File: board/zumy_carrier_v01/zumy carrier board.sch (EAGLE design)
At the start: 16 parts, among them J1 ODROID_POWER, J2 BATT_POWER, M1 POLOLU_STEP_DOWN, M2 ITG/MPU_MODULE, M3 POLOLU_DRV8833_MODULE, SW1 500SSP1S1M6QEA

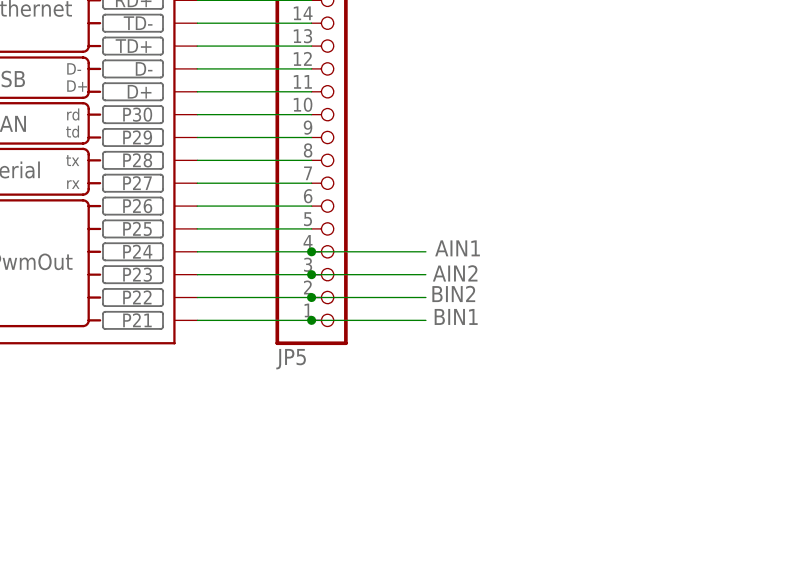
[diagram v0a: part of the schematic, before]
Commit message: Most of Rev D done. Major rearrangement. New mounting hole pattern.
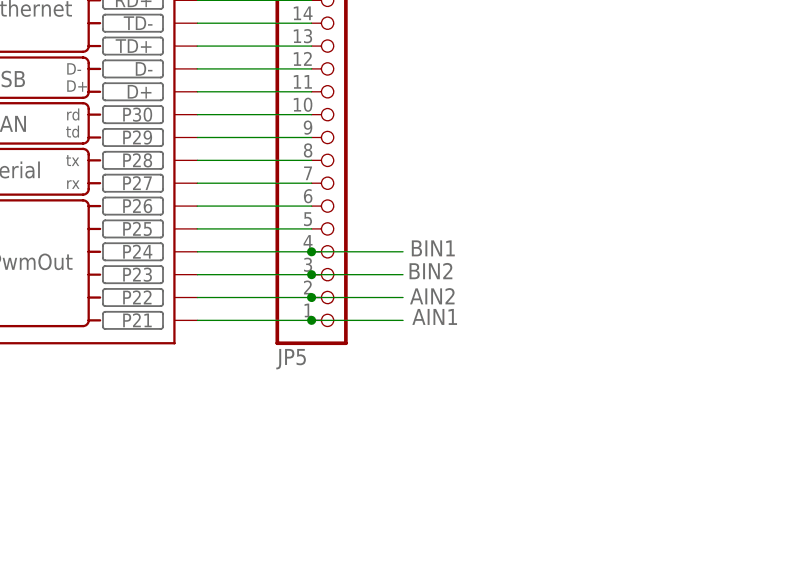
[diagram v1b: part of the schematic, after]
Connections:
- net AIN1: now also JP5.1, KIT1.P21; no longer JP5.4, KIT1.P24
- net AIN2: now also JP5.2, KIT1.P22; no longer JP5.3, KIT1.P23
- net BIN1: now also JP5.4, KIT1.P24; no longer JP5.1, KIT1.P21
- net BIN2: now also JP5.3, KIT1.P23; no longer JP5.2, KIT1.P22
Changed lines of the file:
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@@
 </segment>
 <segment>
-<pinref part="JP5" gate="A" pin="1"/>
-<wire x1="167.64" y1="58.42" x2="180.34" y2="58.42" width="0.1524" layer="91"/>
-<wire x1="180.34" y1="58.42" x2="193.04" y2="58.42" width="0.1524" layer="91"/>
-<junction x="180.34" y="58.42"/>
-<label x="193.802" y="57.912" size="1.778" layer="95"/>
-<pinref part="KIT1" gate="KIT" pin="P21"/>
+<pinref part="JP5" gate="A" pin="4"/>
+<wire x1="167.64" y1="66.04" x2="180.34" y2="66.04" width="0.1524" layer="91"/>
+<pinref part="KIT1" gate="KIT" pin="P24"/>
+<wire x1="180.34" y1="66.04" x2="190.5" y2="66.04" width="0.1524" layer="91"/>
+<label x="191.262" y="65.532" size="1.778" layer="95"/>
+<junction x="180.34" y="66.04"/>
 </segment>
 </net>
@@
 </segment>
 <segment>
-<pinref part="JP5" gate="A" pin="2"/>
-<wire x1="167.64" y1="60.96" x2="180.34" y2="60.96" width="0.1524" layer="91"/>
-<wire x1="180.34" y1="60.96" x2="193.04" y2="60.96" width="0.1524" layer="91"/>
-<junction x="180.34" y="60.96"/>
-<label x="193.548" y="60.452" size="1.778" layer="95"/>
-<pinref part="KIT1" gate="KIT" pin="P22"/>
+<pinref part="JP5" gate="A" pin="3"/>
+<wire x1="167.64" y1="63.5" x2="180.34" y2="63.5" width="0.1524" layer="91"/>
+<pinref part="KIT1" gate="KIT" pin="P23"/>
+<wire x1="180.34" y1="63.5" x2="190.5" y2="63.5" width="0.1524" layer="91"/>
+<label x="191.008" y="62.992" size="1.778" layer="95"/>
+<junction x="180.34" y="63.5"/>
 </segment>
 </net>
@@
 </segment>
 <segment>
-<pinref part="JP5" gate="A" pin="3"/>
-<wire x1="167.64" y1="63.5" x2="180.34" y2="63.5" width="0.1524" layer="91"/>
-<wire x1="180.34" y1="63.5" x2="193.04" y2="63.5" width="0.1524" layer="91"/>
-<junction x="180.34" y="63.5"/>
-<label x="193.802" y="62.738" size="1.778" layer="95"/>
-<pinref part="KIT1" gate="KIT" pin="P23"/>
+<pinref part="JP5" gate="A" pin="2"/>
+<wire x1="167.64" y1="60.96" x2="180.34" y2="60.96" width="0.1524" layer="91"/>
+<pinref part="KIT1" gate="KIT" pin="P22"/>
+<wire x1="180.34" y1="60.96" x2="190.5" y2="60.96" width="0.1524" layer="91"/>
+<label x="191.262" y="60.198" size="1.778" layer="95"/>
+<junction x="180.34" y="60.96"/>
 </segment>
 </net>
@@
 </segment>
 <segment>
-<pinref part="JP5" gate="A" pin="4"/>
-<wire x1="167.64" y1="66.04" x2="180.34" y2="66.04" width="0.1524" layer="91"/>
-<wire x1="180.34" y1="66.04" x2="193.04" y2="66.04" width="0.1524" layer="91"/>
-<junction x="180.34" y="66.04"/>
-<label x="194.056" y="65.532" size="1.778" layer="95"/>
-<pinref part="KIT1" gate="KIT" pin="P24"/>
+<pinref part="JP5" gate="A" pin="1"/>
+<wire x1="167.64" y1="58.42" x2="180.34" y2="58.42" width="0.1524" layer="91"/>
+<pinref part="KIT1" gate="KIT" pin="P21"/>
+<wire x1="180.34" y1="58.42" x2="190.5" y2="58.42" width="0.1524" layer="91"/>
+<label x="191.516" y="57.912" size="1.778" layer="95"/>
+<junction x="180.34" y="58.42"/>
 </segment>
 </net>

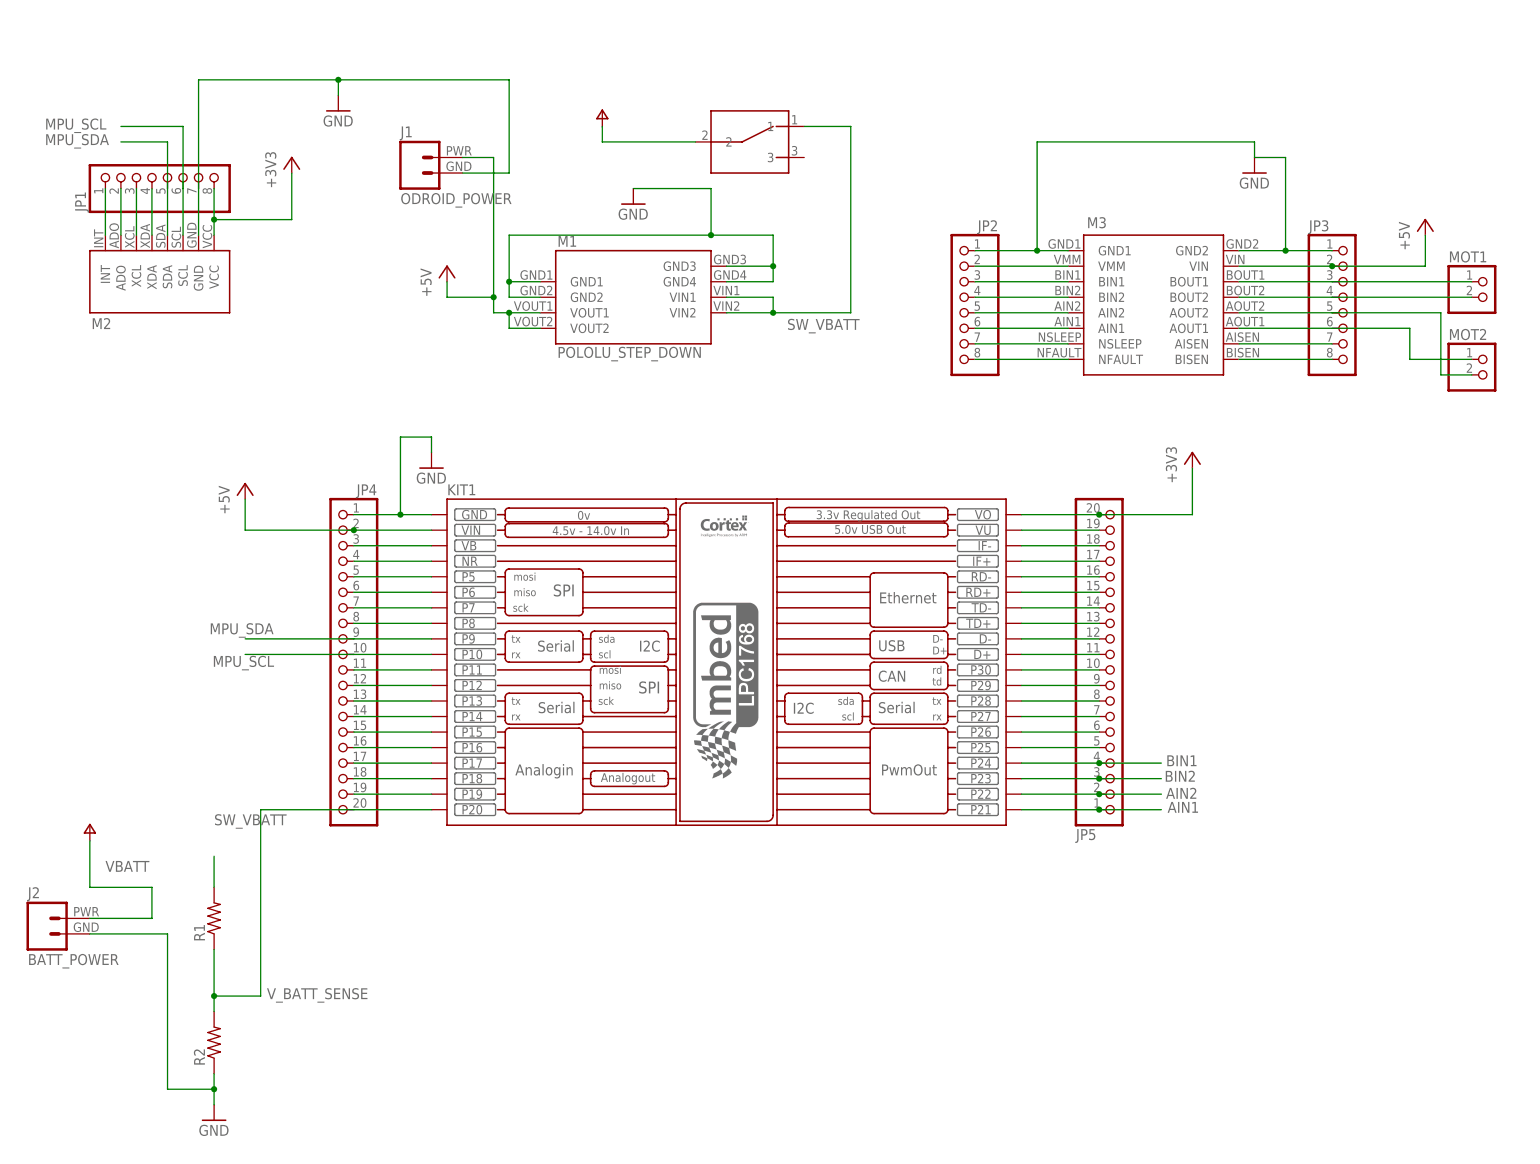
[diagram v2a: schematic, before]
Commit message: Added 6pin shrouded connectors for pololu encoder + motor drive. Routing is all screwed up.
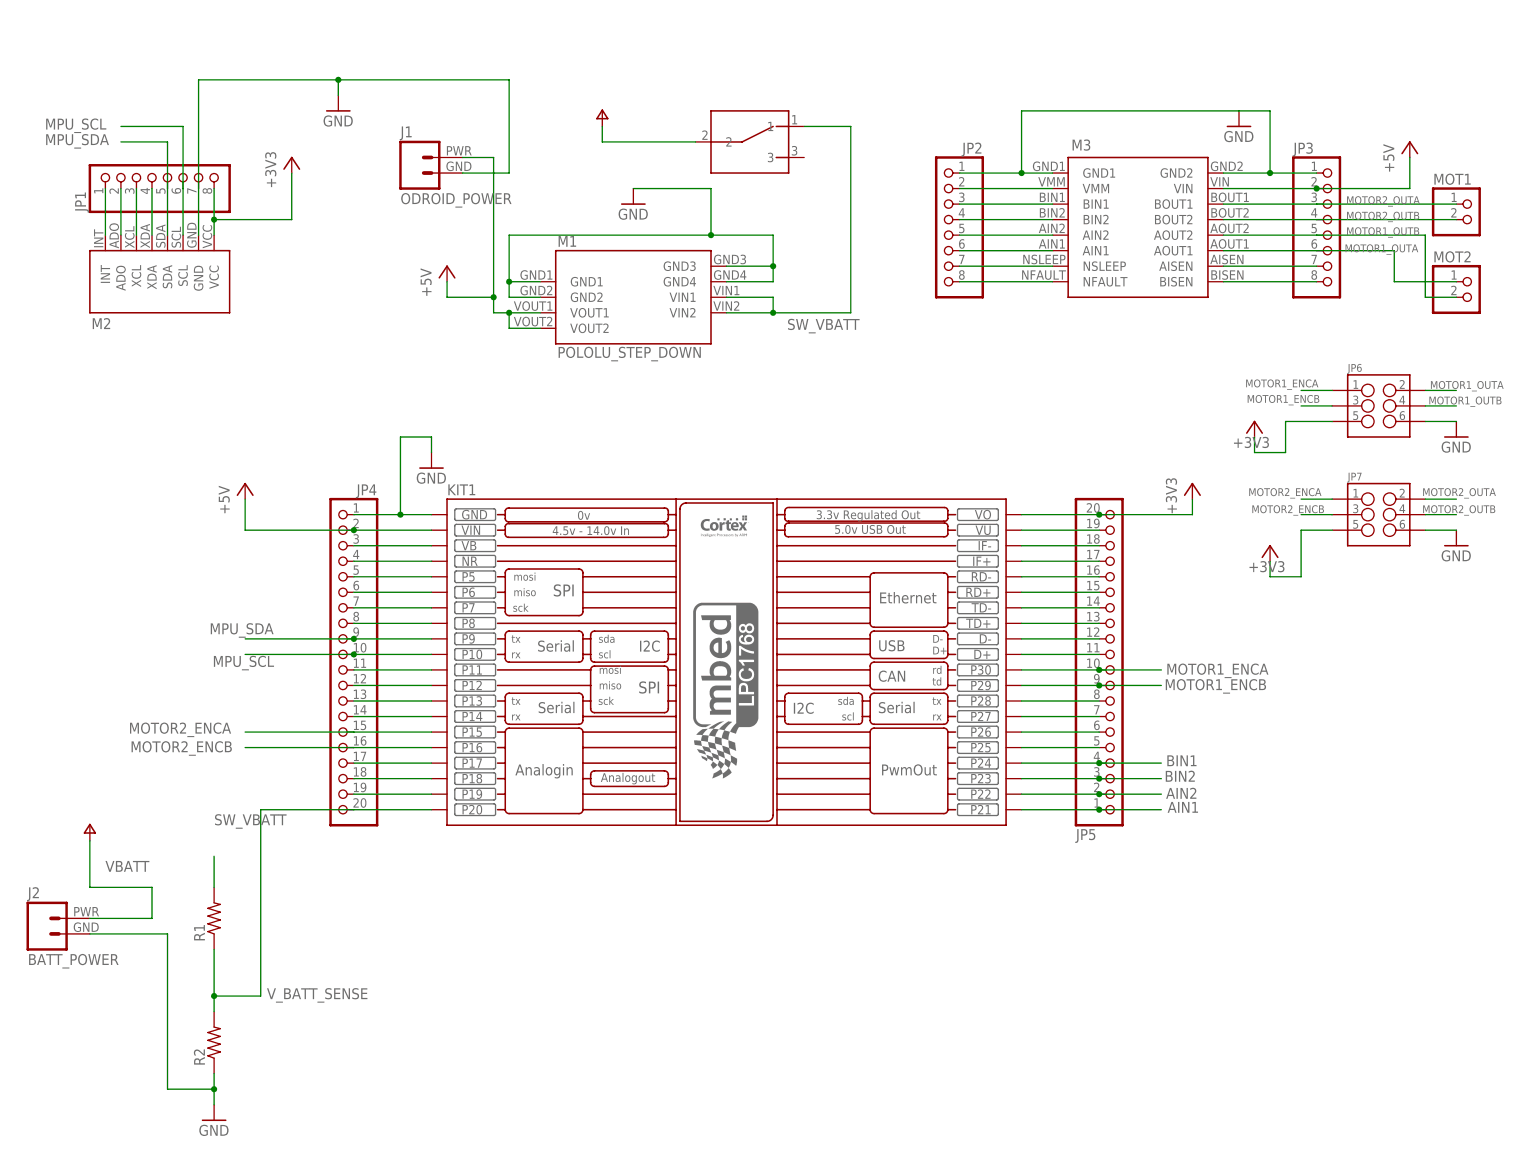
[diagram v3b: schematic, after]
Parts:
- added JP6, JP7: (no value), SparkFun-Connectors:M03X2SHROUD
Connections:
- removed net N$10: JP4.15, KIT1.P15
- removed net N$24: JP4.16, KIT1.P16
- removed net N$37: JP5.9, KIT1.P29
- removed net N$38: JP5.10, KIT1.P30
- removed net N$59: JP3.3, M3.BOUT1, MOT1.1
- removed net N$60: JP3.4, M3.BOUT2, MOT1.2
- removed net N$61: JP3.5, M3.AOUT2, MOT2.2
- removed net N$62: JP3.6, M3.AOUT1, MOT2.1
- new net MOTOR1_ENCA: JP5.10, JP6.1, KIT1.P30
- new net MOTOR1_ENCB: JP5.9, JP6.3, KIT1.P29
- new net MOTOR1_OUTA: JP3.6, JP6.2, M3.AOUT1, MOT2.1
- new net MOTOR1_OUTB: JP3.5, JP6.4, M3.AOUT2, MOT2.2
- new net MOTOR2_ENCA: JP4.15, JP7.1, KIT1.P15
- new net MOTOR2_ENCB: JP4.16, JP7.3, KIT1.P16
- new net MOTOR2_OUTA: JP3.3, JP7.2, M3.BOUT1, MOT1.1
- new net MOTOR2_OUTB: JP3.4, JP7.4, M3.BOUT2, MOT1.2
- net +3V3: now also JP6.5, JP7.5
- net GND: now also JP6.6, JP7.6
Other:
- moved on the sheet: JP2, JP3, M3, MOT1, MOT2

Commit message: Rev D now with encoder connectors, fully routed, no DRC errors.
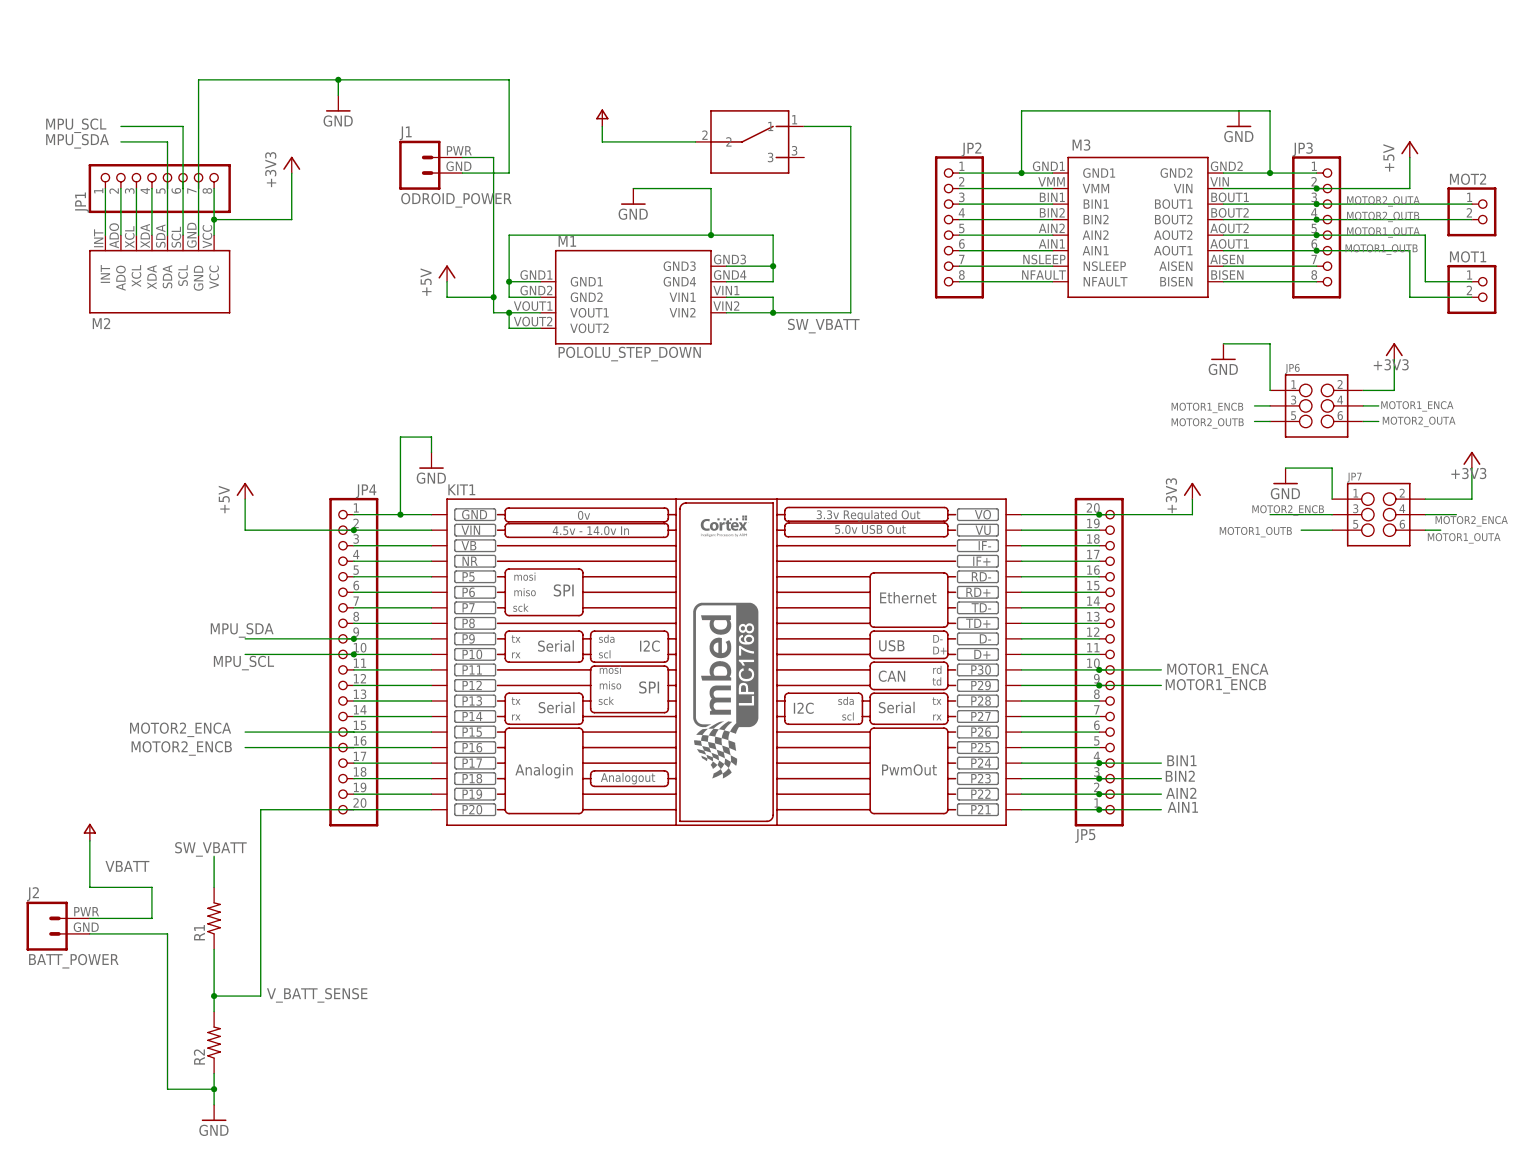
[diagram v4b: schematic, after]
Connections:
- net +3V3: now also JP6.2, JP7.2; no longer JP6.5, JP7.5
- net GND: now also JP6.1, JP7.1; no longer JP6.6, JP7.6
- net MOTOR1_ENCA: now also JP6.4; no longer JP6.1
- net MOTOR1_OUTA: now also JP3.5, JP7.6, M3.AOUT2, MOT1.1; no longer JP3.6, JP6.2, M3.AOUT1, MOT2.1
- net MOTOR1_OUTB: now also JP3.6, JP7.5, M3.AOUT1, MOT1.2; no longer JP3.5, JP6.4, M3.AOUT2, MOT2.2
- net MOTOR2_ENCA: now also JP7.4; no longer JP7.1
- net MOTOR2_OUTA: now also JP6.6, MOT2.1; no longer JP7.2, MOT1.1
- net MOTOR2_OUTB: now also JP6.5, MOT2.2; no longer JP7.4, MOT1.2
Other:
- moved on the sheet: JP6, MOT1, MOT2

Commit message: Rev D routed with schmitt triggers on encoders.
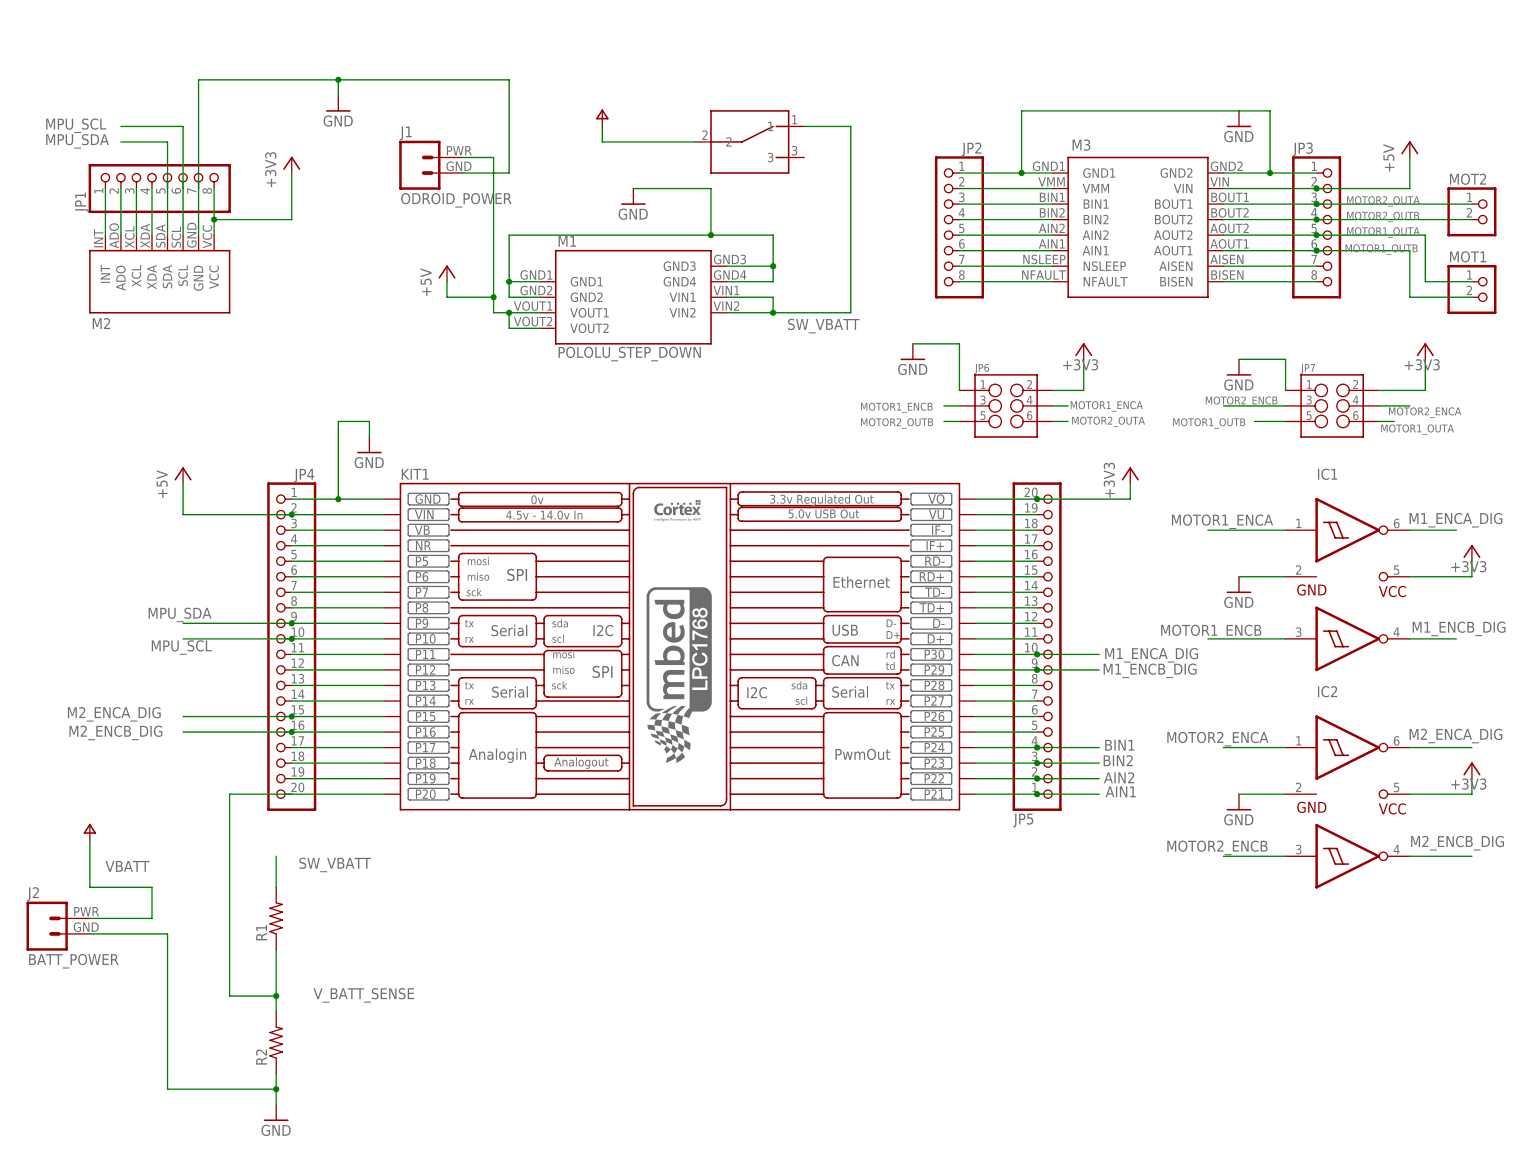
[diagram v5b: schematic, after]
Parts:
- added IC1, IC2: SN74AUP2G17, zumy:SN74AUP2G17
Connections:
- new net M1_ENCA_DIG: IC1.1Y, JP5.10, KIT1.P30
- new net M1_ENCB_DIG: IC1.2Y, JP5.9, KIT1.P29
- new net M2_ENCA_DIG: IC2.1Y, JP4.15, KIT1.P15
- new net M2_ENCB_DIG: IC2.2Y, JP4.16, KIT1.P16
- net +3V3: now also IC1.VCC, IC2.VCC
- net GND: now also IC1.GND, IC2.GND
- net MOTOR1_ENCA: now also IC1.1A; no longer JP5.10, KIT1.P30
- net MOTOR1_ENCB: now also IC1.2A; no longer JP5.9, KIT1.P29
- net MOTOR2_ENCA: now also IC2.1A; no longer JP4.15, KIT1.P15
- net MOTOR2_ENCB: now also IC2.2A; no longer JP4.16, KIT1.P16
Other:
- moved on the sheet: JP4, JP5, JP6, JP7, KIT1, R1, R2
